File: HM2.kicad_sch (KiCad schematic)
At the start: 3 parts

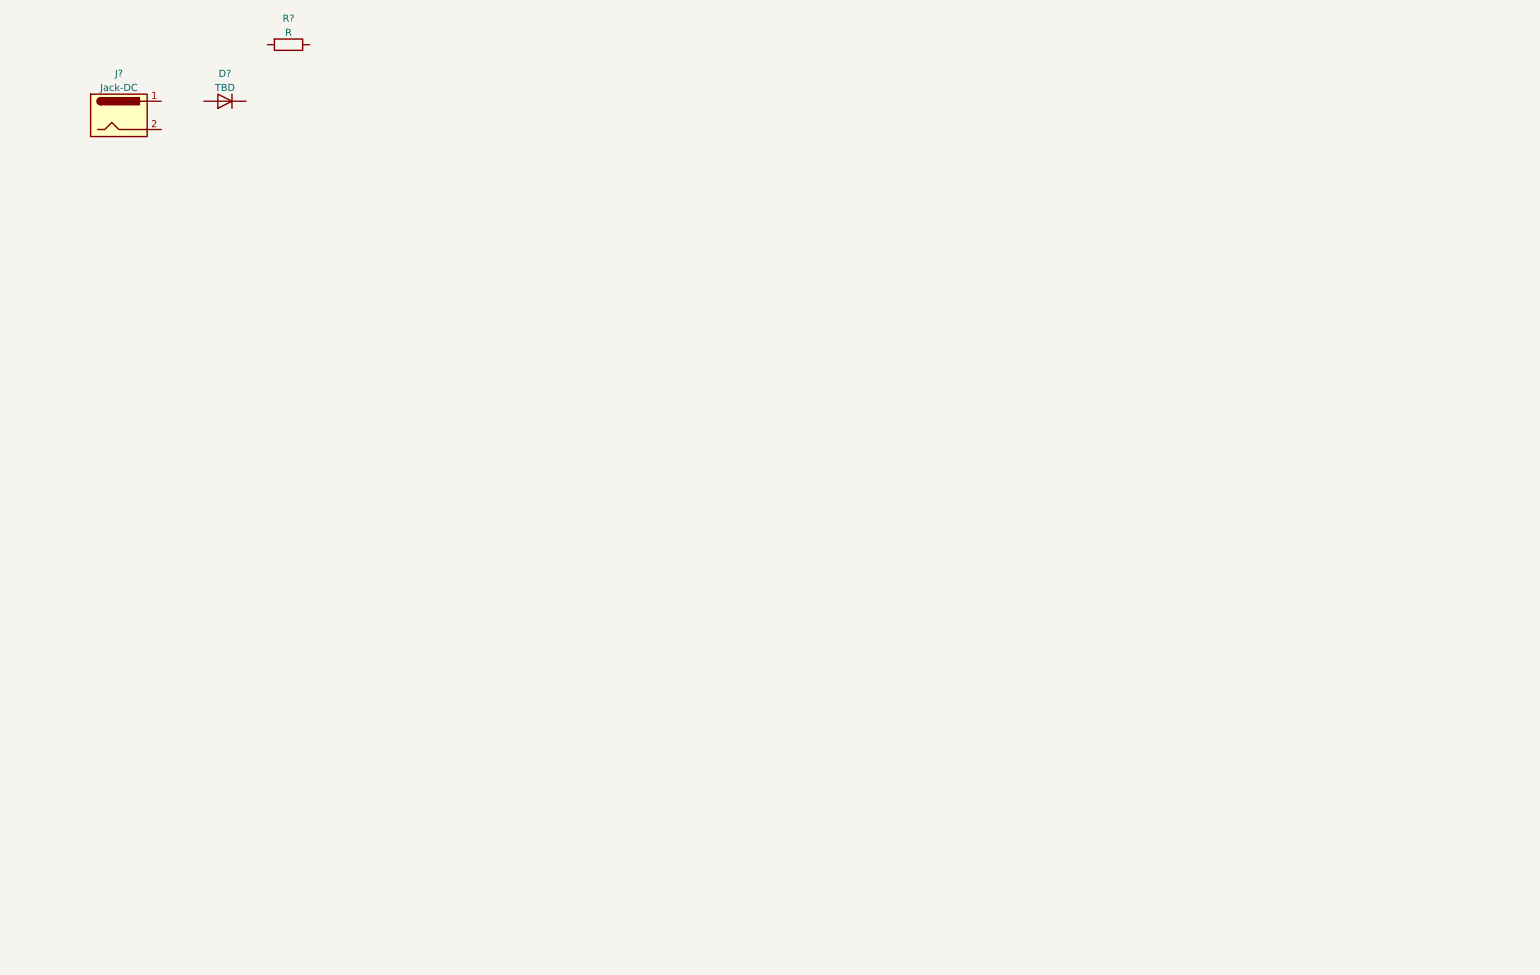
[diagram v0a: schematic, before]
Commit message: pcb routed
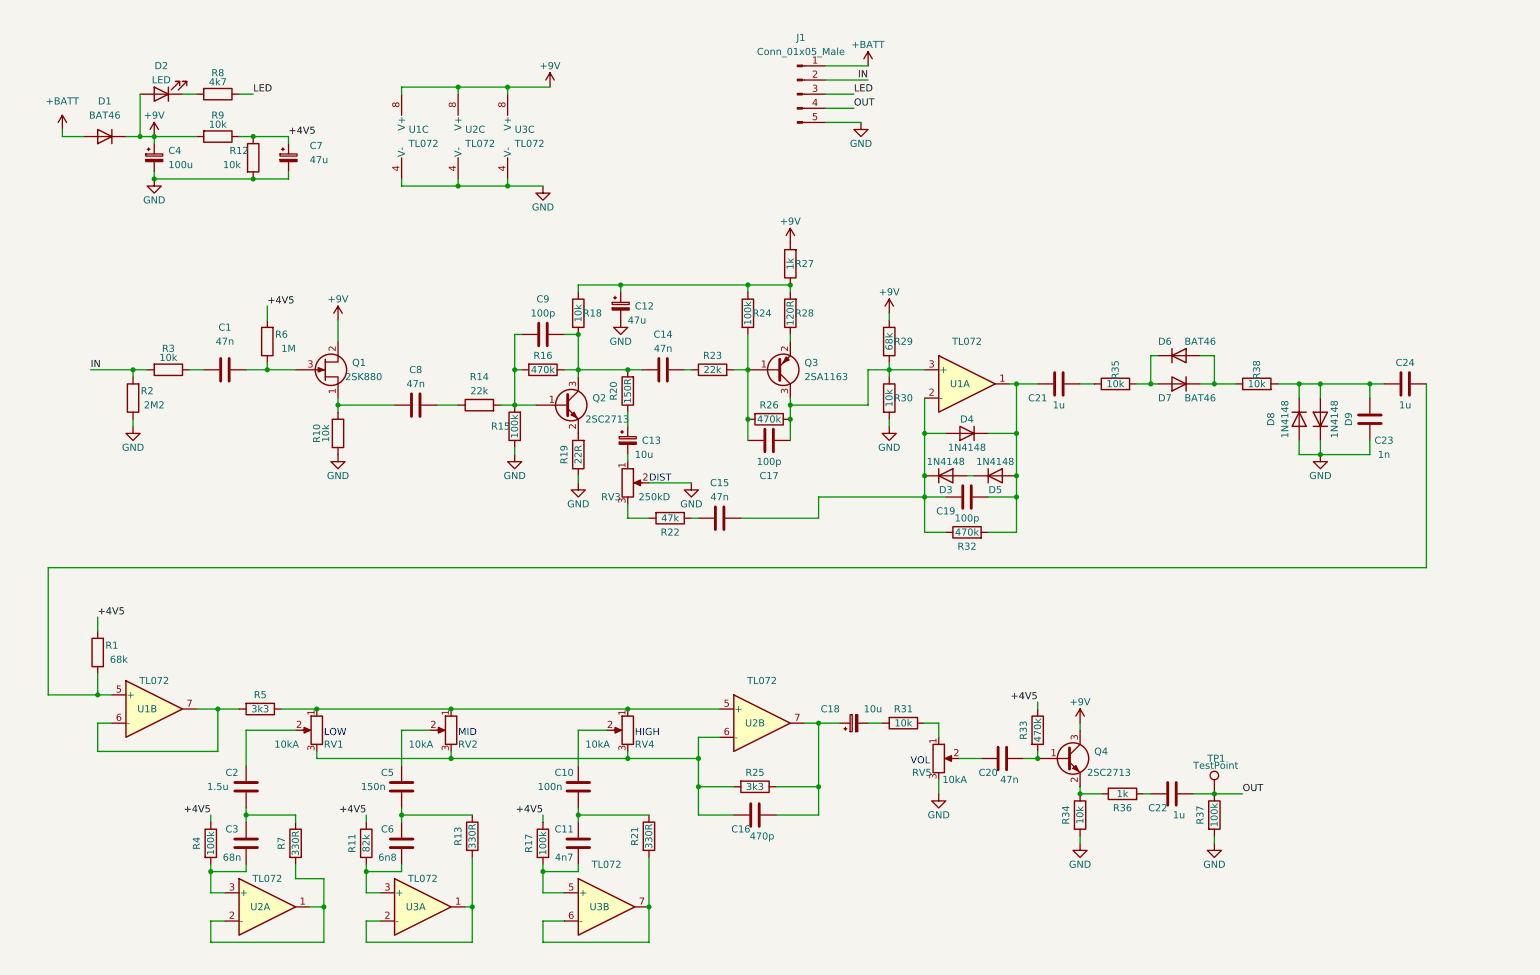
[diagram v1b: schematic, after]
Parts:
- removed J?: Jack-DC, symbol Connector:Jack-DC
- added C1, C14, C15, C20, C8: 47n, Capacitor_SMD:C_0805_2012Metric_Pad1.18x1.45mm_HandSolder, symbol Device:C
- added C10: 100n, Capacitor_SMD:C_0805_2012Metric_Pad1.18x1.45mm_HandSolder, symbol Device:C
- added C11: 4n7, Capacitor_SMD:C_0805_2012Metric_Pad1.18x1.45mm_HandSolder, symbol Device:C
- added C12, C7: 47u, Capacitor_SMD:CP_Elec_6.3x5.4, symbol Device:C_Polarized_Small
- added C13, C18: 10u, Capacitor_SMD:CP_Elec_5x5.4, symbol Device:C_Polarized_Small
- added C16: 470p, Capacitor_SMD:C_0805_2012Metric_Pad1.18x1.45mm_HandSolder, symbol Device:C
- added C17, C19, C9: 100p, Capacitor_SMD:C_0805_2012Metric_Pad1.18x1.45mm_HandSolder, symbol Device:C
- added C2: 1.5u, Capacitor_SMD:C_0805_2012Metric_Pad1.18x1.45mm_HandSolder, symbol Device:C
- added C21, C22, C24: 1u, Capacitor_SMD:C_0805_2012Metric_Pad1.18x1.45mm_HandSolder, symbol Device:C
- added C23: 1n, Capacitor_SMD:C_0805_2012Metric_Pad1.18x1.45mm_HandSolder, symbol Device:C
- added C3: 68n, Capacitor_SMD:C_0805_2012Metric_Pad1.18x1.45mm_HandSolder, symbol Device:C
- added C4: 100u, Capacitor_SMD:CP_Elec_6.3x7.7, symbol Device:C_Polarized_Small
- added C5: 150n, Capacitor_SMD:C_0805_2012Metric_Pad1.18x1.45mm_HandSolder, symbol Device:C
- added C6: 6n8, Capacitor_SMD:C_0805_2012Metric_Pad1.18x1.45mm_HandSolder, symbol Device:C
- added D2: LED, LED_THT:LED_D3.0mm, symbol Device:LED
- added D3, D4, D5, D8, D9: 1N4148, Diode_SMD:D_SOD-123, symbol Device:D
- added D6, D7: BAT46, Diode_SMD:D_SOD-123, symbol Device:D
- added J1: Conn_01x05_Male, Connector_PinSocket_2.54mm:PinSocket_1x05_P2.54mm_Vertical, symbol Connector:Conn_01x05_Male
- added Q1: 2SK880, Package_TO_SOT_SMD:SOT-323_SC-70_Handsoldering, symbol Device:Q_NJFET_SDG
- added Q2, Q4: 2SC2713, Package_TO_SOT_SMD:SOT-23, symbol Device:Q_NPN_BEC
- added Q3: 2SA1163, Package_TO_SOT_SMD:SOT-23, symbol Device:Q_PNP_BEC
- added R1, R29: 68k, Resistor_SMD:R_0805_2012Metric_Pad1.20x1.40mm_HandSolder, symbol Device:R
- added R10, R12, R18, R3, R30, R31, R34, R35, R38, R9: 10k, Resistor_SMD:R_0805_2012Metric_Pad1.20x1.40mm_HandSolder, symbol Device:R
- added R11: 82k, Resistor_SMD:R_0805_2012Metric_Pad1.20x1.40mm_HandSolder, symbol Device:R
- added R13, R21, R7: 330R, Resistor_SMD:R_0805_2012Metric_Pad1.20x1.40mm_HandSolder, symbol Device:R
- added R14, R23: 22k, Resistor_SMD:R_0805_2012Metric_Pad1.20x1.40mm_HandSolder, symbol Device:R
- added R15, R17, R24, R37, R4: 100k, Resistor_SMD:R_0805_2012Metric_Pad1.20x1.40mm_HandSolder, symbol Device:R
- added R16, R26, R32, R33: 470k, Resistor_SMD:R_0805_2012Metric_Pad1.20x1.40mm_HandSolder, symbol Device:R
- added R19: 22R, Resistor_SMD:R_0805_2012Metric_Pad1.20x1.40mm_HandSolder, symbol Device:R
- added R2: 2M2, Resistor_SMD:R_0805_2012Metric_Pad1.20x1.40mm_HandSolder, symbol Device:R
- added R20: 150R, Resistor_SMD:R_0805_2012Metric_Pad1.20x1.40mm_HandSolder, symbol Device:R
- added R22: 47k, Resistor_SMD:R_0805_2012Metric_Pad1.20x1.40mm_HandSolder, symbol Device:R
- added R25, R5: 3k3, Resistor_SMD:R_0805_2012Metric_Pad1.20x1.40mm_HandSolder, symbol Device:R
- added R27, R36: 1k, Resistor_SMD:R_0805_2012Metric_Pad1.20x1.40mm_HandSolder, symbol Device:R
- added R28: 120R, Resistor_SMD:R_0805_2012Metric_Pad1.20x1.40mm_HandSolder, symbol Device:R
- added R6: 1M, Resistor_SMD:R_0805_2012Metric_Pad1.20x1.40mm_HandSolder, symbol Device:R
- added RV1, RV2, RV4, RV5: 10kA, Connector_PinHeader_2.54mm:PinHeader_1x03_P2.54mm_Vertical, symbol Device:R_Potentiometer
- added RV3: 250kD, Connector_PinHeader_2.54mm:PinHeader_1x03_P2.54mm_Vertical, symbol Device:R_Potentiometer
- added TP1: TestPoint, TestPoint:TestPoint_Pad_D1.5mm, symbol Connector:TestPoint
- added U1, U2, U3: TL072, Package_SO:SOIC-8_3.9x4.9mm_P1.27mm, symbol Amplifier_Operational:TL072
- D1: renamed from D?; value TBD -> BAT46; footprint (none) -> Diode_SMD:D_SOD-123
- R8: renamed from R?; value R -> 4k7; footprint (none) -> Resistor_SMD:R_0805_2012Metric_Pad1.20x1.40mm_HandSolder
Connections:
- net LED: now reaches R8.1
- net LED: now also J1.3 (Pin_3)
- net at R8.2: now also D2.1 (K)
- net +9V: now reaches D1.1 (K)
- net +9V: now also C4.1, D2.2 (A), Q1.2 (D), Q4.3 (C), R27.2, R29.1, R9.2, U1.8 (V+), U2.8 (V+), U3.8 (V+)
- net +BATT: now reaches D1.2 (A)
- net +BATT: now also J1.1 (Pin_1)
- new net: C11.1, R17.2, U3.5 (+)
- new net: R21.2, U3.6 (-), U3.7
- new net: R5.1, RV1.1, RV2.1, RV4.1, U2.5 (+)
- new net: C5.2, RV2.2
- new net: C16.2, R25.2, RV1.3, RV2.3, RV4.3, U2.6 (-)
- new net: C1.2, Q1.3 (G), R6.1
- new net: C8.1, Q1.1 (S), R10.1
- new net: C8.2, R14.1
- new net: C16.1, C18.1, R25.1, U2.7
- new net: C18.2, R31.2
- new net: R5.2, U1.6 (-), U1.7
- new net: C15.2, C19.2, D3.1 (K), D4.2 (A), R32.1, U1.2 (-)
- new net: D3.2 (A), D5.1 (K)
- new net: R31.1, RV5.1
- new net: C12.1, R18.1, R24.1, R27.1, R28.2
- new net: C3.1, R4.2, U2.3 (+)
- new net: C2.1, C3.2, R7.1
- new net: C10.2, RV4.2
- new net: C24.1, R1.1, U1.5 (+)
- new net: Q4.2 (E), R34.1, R36.1
- new net: C22.2, R36.2
- new net: C23.1, C24.2, D8.1 (K), D9.2 (A), R38.2
- new net: C13.2, RV3.1
- new net: R22.2, RV3.3
- new net: C9.1, Q2.1 (B), R14.2, R15.2, R16.2
- new net: Q2.2 (E), R19.2
- new net: C14.1, C9.2, Q2.3 (C), R16.1, R18.2, R20.2
- new net: R7.2, U2.1, U2.2 (-)
- new net: D6.2 (A), D7.1 (K), R38.1
- new net: C5.1, C6.2, R13.1
- new net: R13.2, U3.1, U3.2 (-)
- new net: C17.1, Q3.3 (C), R26.1, R29.2, R30.1, U1.3 (+)
- new net: C17.2, Q3.1 (B), R23.2, R24.2, R26.2
- new net: C15.1, R22.1
- new net: C14.2, R23.1
- new net: C2.2, RV1.2
- new net: C10.1, C11.2, R21.1
- new net: C21.1, R35.1
- new net: D6.1 (K), D7.2 (A), R35.2
- new net: C20.2, RV5.2
- new net: C19.1, C21.2, D4.1 (K), D5.2 (A), R32.2, U1.1
- new net: C6.1, R11.2, U3.3 (+)
- new net: Q3.2 (E), R28.1
- new net: C20.1, Q4.1 (B), R33.2
- new net: C13.1, R20.1
- new net: C1.1, R3.1
- new net +4V5: C7.1, R1.2, R11.1, R12.1, R17.1, R33.1, R4.1, R6.2, R9.1
- new net GND: C12.2, C23.2, C4.2, C7.2, D8.2 (A), D9.1 (K), J1.5 (Pin_5), R10.2, R12.2, R15.1, R19.1, R2.1, R30.2, R34.2, R37.2, RV3.2, RV5.3, U1.4 (V-), U2.4 (V-), U3.4 (V-)
- new net IN: J1.2 (Pin_2), R2.2, R3.2
- new net OUT: C22.1, J1.4 (Pin_4), R37.1, TP1.1
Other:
- note added: "DIST"
- note added: "HIGH"
- note added: "LOW"
- note added: "MID"
- note added: "VOL"
- moved on the sheet: D1, R8

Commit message: Schematic revision add decoupling cap on opamp
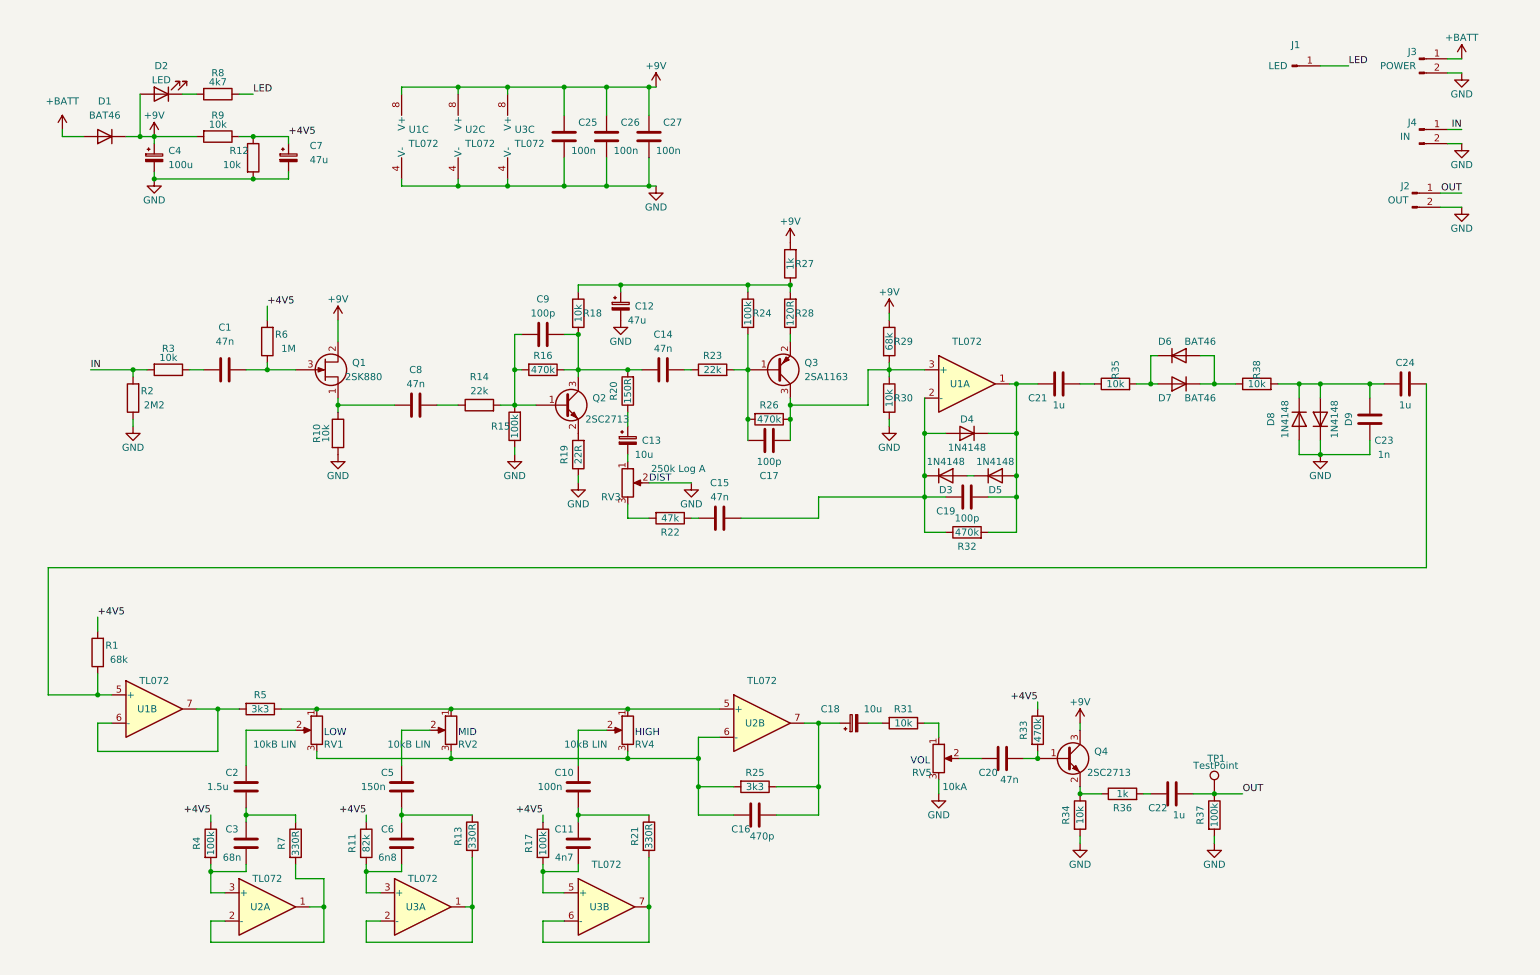
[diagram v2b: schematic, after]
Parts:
- removed J1: Conn_01x05_Male, Connector_PinSocket_2.54mm:PinSocket_1x05_P2.54mm_Vertical, symbol Connector:Conn_01x05_Male
- added C25, C26, C27: 100n, Capacitor_SMD:C_0805_2012Metric_Pad1.18x1.45mm_HandSolder, symbol Device:C
- added J1: LED, symbol Connector:Conn_01x01_Male
- added J2: OUT, symbol Connector:Conn_01x02_Male
- added J3: POWER, symbol Connector:Conn_01x02_Male
- added J4: IN, symbol Connector:Conn_01x02_Male
- RV1, RV2, RV4: value 10kA -> 10kB LIN
- RV3: value 250kD -> 250k Log A
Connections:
- net +9V: now also C25.2, C26.2, C27.2
- net +BATT: now also J3.1 (Pin_1)
- net GND: now also C25.1, C26.1, C27.1, J2.2 (Pin_2), J3.2 (Pin_2), J4.2 (Pin_2)
- net IN: now also J4.1 (Pin_1)
- net LED: now also J1.1 (Pin_1)
- net OUT: now also J2.1 (Pin_1)

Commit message: v3 to production
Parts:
- removed D2: LED, LED_THT:LED_D3.0mm, symbol Device:LED
- removed J1: LED, symbol Connector:Conn_01x01_Male
- removed J2: OUT, symbol Connector:Conn_01x02_Male
- removed J3: POWER, symbol Connector:Conn_01x02_Male
- removed J4: IN, symbol Connector:Conn_01x02_Male
- removed RV1, RV2, RV4: 10kB LIN, Connector_PinHeader_2.54mm:PinHeader_1x03_P2.54mm_Vertical, symbol Device:R_Potentiometer
- added Audio1, Audio2: PJ-603A, AREA_lib_composant:AUDIO-TH_PJ-603A_1, symbol easyeda2kicad:PJ-603A
- added D2: 1N5819WS, Diode_SMD:D_SOD-323, symbol Device:D
- added J2: Barrel_Jack_MountingPin, Connector_BarrelJack:BarrelJack_Horizontal, symbol Connector:Barrel_Jack_MountingPin
- added R39, R40: 0R, Resistor_SMD:R_0603_1608Metric, symbol Device:R
- added R41, R42: 10k, Resistor_SMD:R_0603_1608Metric, symbol Device:R
- added SW1: ~, AREA_lib_composant:3PDT_LED, symbol AREA_composant:3PDT_SW_LED
- C1, C10, C11, C14, C15, C16, C17, C19, C20, C23, C25, C26, C27, C3, C5, C6, C8, C9: footprint Capacitor_SMD:C_0805_2012Metric_Pad1.18x1.45mm_HandSolder -> Capacitor_SMD:C_0603_1608Metric
- C2, C21, C22, C24: footprint Capacitor_SMD:C_0805_2012Metric_Pad1.18x1.45mm_HandSolder -> Capacitor_SMD:C_0805_2012Metric
- D1: value BAT46 -> 1N5819WS; footprint Diode_SMD:D_SOD-123 -> Diode_SMD:D_SOD-323
- D3, D4, D5, D8, D9: footprint Diode_SMD:D_SOD-123 -> Diode_SMD:D_SOD-323
- D6, D7: value BAT46 -> 1N4148; footprint Diode_SMD:D_SOD-123 -> Diode_SMD:D_SOD-323
- Q1: footprint Package_TO_SOT_SMD:SOT-323_SC-70_Handsoldering -> Package_TO_SOT_SMD:SOT-323_SC-70
- R1, R10, R11, R12, R13, R14, R15, R16, R17, R18, R19, R2, R20, R21, R22, R23, R24, R25, R26, R27, R28, R29, R3, R30, R31, R32, R33, R34, R35, R36, R37, R38, R4, R5, R6, R7, R9: footprint Resistor_SMD:R_0805_2012Metric_Pad1.20x1.40mm_HandSolder -> Resistor_SMD:R_0603_1608Metric
- R8: value 4k7 -> 1k; footprint Resistor_SMD:R_0805_2012Metric_Pad1.20x1.40mm_HandSolder -> Resistor_SMD:R_0603_1608Metric
- RV3, RV5: footprint Connector_PinHeader_2.54mm:PinHeader_1x03_P2.54mm_Vertical -> Potentiometer_THT:Potentiometer_Alpha_RD901F-40-00D_Single_Vertical
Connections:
- net +9V: now also D2.1 (K), SW1.8
- net +BATT: now also J2.2
- net GND: now also Audio1.2, Audio2.2, D2.2 (A), J2.1, SW1.10
- net IN: now also Audio2.5, R39.2, SW1.2 (B); no longer R2.2, R3.2
- net OUT: now also Audio1.5, R40.2, SW1.5 (B); no longer C22.1, R37.1, TP1.1
- net at R5.1, U2.5 (+): now also R41.1, R42.1
- net at C5.2: now also C10.2, C16.2, C2.2, R25.2, U2.6 (-), R41.2, R42.2
- net at R8.2: now also SW1.11
- net LED renamed IN_LED
- net IN_LED: now also SW1.9 (C)
- new net: Audio1.4, R40.1
- new net: Audio2.4, R39.1
- new net: SW1.1 (A), SW1.4 (A)
- new net IN_FX: R2.2, R3.2, SW1.3 (C)
- new net OUT_FX: C22.1, R37.1, SW1.6 (C), TP1.1
- no-connect marks 0 -> 2
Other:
- note added: "Maxed pot replaced by resistors"
- note removed: "HIGH"
- note removed: "LOW"
- note removed: "MID"
- moved on the sheet: C1, C10, C11, C12, C13, C14, C15, C17, C19, C2, C21, C23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

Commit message: V5 layout to review
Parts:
- removed D2: 1N5819WS, Diode_SMD:D_SOD-323, symbol Device:D
- removed Q2, Q4: 2SC2713, Package_TO_SOT_SMD:SOT-23, symbol Device:Q_NPN_BEC
- removed Q3: 2SA1163, Package_TO_SOT_SMD:SOT-23, symbol Device:Q_PNP_BEC
- removed R39, R40: 0R, Resistor_SMD:R_0603_1608Metric, symbol Device:R
- added C28: 100n, Capacitor_SMD:C_0603_1608Metric, symbol Device:C
- added C29: 10n, Capacitor_SMD:C_0603_1608Metric, symbol Device:C
- added Q2: 2N3906, Package_TO_SOT_SMD:SOT-23-3, symbol Transistor_BJT:2N3906
- added Q3, Q5: 2N3904, Package_TO_SOT_SMD:SOT-23-3, symbol Transistor_BJT:2N3904
- C12: footprint Capacitor_SMD:CP_Elec_6.3x5.4 -> Capacitor_SMD:CP_Elec_4x5.8
- C4: value 100u -> 470u; footprint Capacitor_SMD:CP_Elec_6.3x7.7 -> Capacitor_SMD:CP_Elec_10x10
- C7: footprint Capacitor_SMD:CP_Elec_6.3x5.4 -> Capacitor_SMD:CP_Elec_6.3x5.8
- Q1: value 2SK880 -> MMBFJ201; footprint Package_TO_SOT_SMD:SOT-323_SC-70 -> Package_TO_SOT_SMD:SOT-23-3; symbol Device:Q_NJFET_SDG -> Device:Q_NJFET_DSG
- R32: value 470k -> 220k
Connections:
- net +9V: now also Q1.1 (D), R8.1, C28.2, C29.2, Q3.3 (C); no longer Q1.2 (D), SW1.8
- net GND: now also Audio1.5, Audio2.5, SW1.4 (A), SW1.5 (B), C28.1, C29.1; no longer SW1.10
- net IN: now also Audio1.4, SW1.8; no longer Audio2.5, SW1.2 (B)
- net IN_FX: now also SW1.9 (C); no longer SW1.3 (C)
- net OUT: now also Audio2.4, SW1.2 (B); no longer Audio1.5, SW1.5 (B)
- net OUT_FX: now also SW1.3 (C); no longer SW1.6 (C)
- net at C8.1, R10.1: now also Q1.2 (S); no longer Q1.1 (S)
- net at R34.1, R36.1: now also Q3.1 (E)
- net at RV3.1: now also R20.1; no longer C13.2
- net at C9.1, R14.2, R15.2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: now also Q5.2 (B)
- net at R19.2: now also Q5.1 (E)
- net at C14.1, C9.2, R16.1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: now also C13.1, Q5.3 (C); no longer R20.2
- net at C17.1, R26.1, R29.2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: now also Q2.3 (C)
- net at C17.2, R23.2, R24.2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: now also Q2.2 (B)
- net at R28.1: now also Q2.1 (E)
- net at C20.1, R33.2: now also Q3.2 (B)
- net at SW1.1 (A): now also SW1.7 (A); no longer SW1.4 (A)
- removed net IN_LED: R8.1, SW1.9 (C)
- new net: C13.2, R20.2
- new net GND_LED: SW1.10, SW1.6 (C)
- no-connect marks 2 -> 1
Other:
- moved on the sheet: C13, C23, C4, C7, D1, D8, D9, J2, R12, R20, R38, R8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

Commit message: Added mecanical drawing and new pdf schem
v5 working
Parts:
- removed Q3: 2N3904, Package_TO_SOT_SMD:SOT-23-3, symbol Transistor_BJT:2N3904
- added C30: 100p, Capacitor_SMD:C_0603_1608Metric, symbol Device:C
- added Q3: MMBT3904, Package_TO_SOT_SMD:SOT-23, symbol Transistor_BJT:MMBT3904
- C4: value 470u -> 220u; footprint Capacitor_SMD:CP_Elec_10x10 -> Capacitor_SMD:CP_Elec_6.3x7.7
- Q2: value 2N3906 -> MMBT3906; footprint Package_TO_SOT_SMD:SOT-23-3 -> Package_TO_SOT_SMD:SOT-23; symbol Transistor_BJT:2N3906 -> Transistor_BJT:MMBT3906
- Q5: value 2N3904 -> MMBT3904; footprint Package_TO_SOT_SMD:SOT-23-3 -> Package_TO_SOT_SMD:SOT-23; symbol Transistor_BJT:2N3904 -> Transistor_BJT:MMBT3904
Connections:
- net +9V: now also Q3.3 (C)
- net GND: now also C30.2
- net GND_LED: now also SW1.12
- net at R34.1, R36.1: now also Q3.2 (E)
- net at R19.2: now also Q5.2 (E); no longer Q5.1 (E)
- net at C9.1, R14.2, R15.2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: now also Q5.1 (B); no longer Q5.2 (B)
- net at C17.2, R23.2, R24.2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: now also Q2.1 (B), C30.1; no longer Q2.2 (B)
- net at R28.1: now also Q2.2 (E); no longer Q2.1 (E)
- net at C20.1, R33.2: now also Q3.1 (B)
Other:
- moved on the sheet: C14, R19, R23
